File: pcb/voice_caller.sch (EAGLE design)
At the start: 13 parts, among them IC1 MEGA8-AI, IC2 78L12SMD, U1 AT45DB321D-S, X2 RJ45-8L-B

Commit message: Who knows
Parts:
- removed C4: (no value), rcl:C-EUC1206K
- removed IC1: MEGA8-AI, atmel:MEGA8-AI
- removed R3: 220, rcl:R-EU_M1206
- U$1: value MAX4544-EUTSOT23-6 -> NANO-NOISP; device max4544:MAX4544-EUTSOT23-6 -> Arduino-clone:NANO-NOISP
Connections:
- removed net AUDIO: U$1.NO
- removed net MIC_IN: U$1.NC
- removed net MIC_OUT: U$1.COM
- removed net MIC_SWITCH: U$1.IN
- removed net N$2: C4.1, R3.1, U$1.V+
- net +5V: no longer IC1.VCC@1, IC1.VCC@2, R3.2
- net FLASH_CS: no longer IC1.PB2(SS/OC1B)
- net GND: no longer C4.2, IC1.GND, IC1.GND@1, IC1.GND@2, U$1.GND
- net MISO: no longer IC1.PB4(MISO)
- net MOSI: no longer IC1.PB3(MOSI/OC2)
- net SCK: no longer IC1.PB5(SCK)
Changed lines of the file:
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@@
 <?xml version="1.0" encoding="utf-8"?>
 <!DOCTYPE eagle SYSTEM "eagle.dtd">
-<eagle version="7.1.0">
+<eagle version="7.7.0">
 <drawing>
 <settings>
@@
 </classes>
 <parts>
-<part name="IC1" library="atmel" deviceset="MEGA8" device="-AI"/>
 <part name="+8V" library="supply1" deviceset="VCC" device="" value="+8V"/>
 <part name="GND1" library="supply1" deviceset="GND" device=""/>
@@
 <part name="R1" library="rcl" deviceset="R-EU_" device="M1206" value="3k9"/>
 <part name="R2" library="rcl" deviceset="R-EU_" device="M1206" value="2k2"/>
-<part name="U$1" library="max4544" deviceset="MAX4544-EUT" device="SOT23-6"/>
-<part name="R3" library="rcl" deviceset="R-EU_" device="M1206" value="220"/>
-<part name="P+3" library="supply1" deviceset="+5V" device=""/>
-<part name="C4" library="rcl" deviceset="C-EU" device="C1206K"/>
-<part name="GND4" library="supply1" deviceset="GND" device=""/>
-<part name="GND5" library="supply1" deviceset="GND" device=""/>
+<part name="U$1" library="Arduino-clone" deviceset="NANO-NOISP" device=""/>
 </parts>
 <sheets>
@@
 </plain>
 <instances>
-<instance part="IC1" gate="G$1" x="76.2" y="45.72"/>
 <instance part="+8V" gate="VCC" x="25.4" y="99.06"/>
 <instance part="GND1" gate="1" x="25.4" y="81.28"/>
@@
 <instance part="R1" gate="G$1" x="-15.24" y="93.98"/>
 <instance part="R2" gate="G$1" x="-15.24" y="88.9"/>
-<instance part="U$1" gate="G$1" x="15.24" y="137.16"/>
-<instance part="R3" gate="G$1" x="15.24" y="170.18" rot="R90"/>
-<instance part="P+3" gate="1" x="15.24" y="180.34"/>
-<instance part="C4" gate="G$1" x="22.86" y="157.48"/>
-<instance part="GND4" gate="1" x="15.24" y="119.38"/>
-<instance part="GND5" gate="1" x="22.86" y="147.32"/>
+<instance part="U$1" gate="G$1" x="12.7" y="144.78"/>
 </instances>
 <busses>
@@
 <net name="+5V" class="0">
 <segment>
-<pinref part="IC1" gate="G$1" pin="VCC@1"/>
-<wire x1="53.34" y1="35.56" x2="50.8" y2="35.56" width="0.1524" layer="91"/>
-<label x="50.8" y="35.56" size="1.27" layer="95" rot="R180" xref="yes"/>
-</segment>
-<segment>
-<pinref part="IC1" gate="G$1" pin="VCC@2"/>
-<wire x1="53.34" y1="33.02" x2="50.8" y2="33.02" width="0.1524" layer="91"/>
-<label x="50.8" y="33.02" size="1.27" layer="95" rot="R180" xref="yes"/>
-</segment>
-<segment>
 <pinref part="P+2" gate="1" pin="+5V"/>
 <pinref part="C2" gate="G$1" pin="1"/>
@@
 <wire x1="48.26" y1="96.52" x2="48.26" y2="93.98" width="0.1524" layer="91"/>
 </segment>
-<segment>
-<pinref part="R3" gate="G$1" pin="2"/>
-<wire x1="15.24" y1="175.26" x2="15.24" y2="177.8" width="0.1524" layer="91"/>
-<pinref part="P+3" gate="1" pin="+5V"/>
-</segment>
 </net>
 <net name="GND" class="0">
-<segment>
-<pinref part="IC1" gate="G$1" pin="GND@1"/>
-<wire x1="53.34" y1="40.64" x2="50.8" y2="40.64" width="0.1524" layer="91"/>
-<label x="50.8" y="40.64" size="1.27" layer="95" rot="R180" xref="yes"/>
-</segment>
-<segment>
-<pinref part="IC1" gate="G$1" pin="GND@2"/>
-<wire x1="53.34" y1="38.1" x2="50.8" y2="38.1" width="0.1524" layer="91"/>
-<label x="50.8" y="38.1" size="1.27" layer="95" rot="R180" xref="yes"/>
-</segment>
 <segment>
 <pinref part="GND1" gate="1" pin="GND"/>
@@
 </segment>
 <segment>
-<pinref part="IC1" gate="G$1" pin="GND"/>
-<wire x1="53.34" y1="66.04" x2="50.8" y2="66.04" width="0.1524" layer="91"/>
-<label x="50.8" y="66.04" size="1.27" layer="95" rot="R180" xref="yes"/>
-</segment>
-<segment>
 <pinref part="U1" gate="G$1" pin="GND"/>
 <wire x1="172.72" y1="63.5" x2="175.26" y2="63.5" width="0.1524" layer="91"/>
@@
 <label x="-25.4" y="48.26" size="1.016" layer="95" xref="yes"/>
 </segment>
-<segment>
-<pinref part="U$1" gate="G$1" pin="GND"/>
-<wire x1="15.24" y1="124.46" x2="15.24" y2="121.92" width="0.1524" layer="91"/>
-<pinref part="GND4" gate="1" pin="GND"/>
-</segment>
-<segment>
-<pinref part="GND5" gate="1" pin="GND"/>
-<pinref part="C4" gate="G$1" pin="2"/>
-<wire x1="22.86" y1="149.86" x2="22.86" y2="152.4" width="0.1524" layer="91"/>
-</segment>
 </net>
 <net name="VCC" class="0">
@@
 <net name="MOSI" class="0">
 <segment>
-<pinref part="IC1" gate="G$1" pin="PB3(MOSI/OC2)"/>
 <wire x1="101.6" y1="17.78" x2="104.14" y2="17.78" width="0.1524" layer="91"/>
 <label x="104.14" y="17.78" size="1.016" layer="95" xref="yes"/>
@@
 <net name="MISO" class="0">
 <segment>
-<pinref part="IC1" gate="G$1" pin="PB4(MISO)"/>
 <wire x1="101.6" y1="15.24" x2="104.14" y2="15.24" width="0.1524" layer="91"/>
 <label x="104.14" y="15.24" size="1.016" layer="95" xref="yes"/>
@@
 <net name="SCK" class="0">
 <segment>
-<pinref part="IC1" gate="G$1" pin="PB5(SCK)"/>
 <wire x1="101.6" y1="12.7" x2="104.14" y2="12.7" width="0.1524" layer="91"/>
 <label x="104.14" y="12.7" size="1.016" layer="95" xref="yes"/>
@@
 </segment>
 <segment>
-<pinref part="IC1" gate="G$1" pin="PB2(SS/OC1B)"/>
 <wire x1="101.6" y1="20.32" x2="104.14" y2="20.32" width="0.1524" layer="91"/>
 <label x="104.14" y="20.32" size="1.016" layer="95" xref="yes"/>
@@
 </segment>
 </net>
-<net name="N$2" class="0">
-<segment>
-<pinref part="U$1" gate="G$1" pin="V+"/>
-<wire x1="15.24" y1="149.86" x2="15.24" y2="162.56" width="0.1524" layer="91"/>
-<pinref part="R3" gate="G$1" pin="1"/>
-<pinref part="C4" gate="G$1" pin="1"/>
-<wire x1="15.24" y1="162.56" x2="15.24" y2="165.1" width="0.1524" layer="91"/>
-<wire x1="22.86" y1="160.02" x2="22.86" y2="162.56" width="0.1524" layer="91"/>
-<wire x1="22.86" y1="162.56" x2="15.24" y2="162.56" width="0.1524" layer="91"/>
-<junction x="15.24" y="162.56"/>
-</segment>
-</net>
-<net name="MIC_OUT" class="0">
-<segment>
-<pinref part="U$1" gate="G$1" pin="COM"/>
-<wire x1="35.56" y1="142.24" x2="38.1" y2="142.24" width="0.1524" layer="91"/>
-<label x="38.1" y="142.24" size="1.016" layer="95" xref="yes"/>
-</segment>
-</net>
-<net name="MIC_SWITCH" class="0">
-<segment>
-<pinref part="U$1" gate="G$1" pin="IN"/>
-<wire x1="35.56" y1="134.62" x2="38.1" y2="134.62" width="0.1524" layer="91"/>
-<label x="38.1" y="134.62" size="1.016" layer="95" xref="yes"/>
-</segment>
-</net>
-<net name="AUDIO" class="0">
-<segment>
-<pinref part="U$1" gate="G$1" pin="NO"/>
-<wire x1="-5.08" y1="134.62" x2="-7.62" y2="134.62" width="0.1524" layer="91"/>
-<label x="-7.62" y="134.62" size="1.016" layer="95" rot="R180" xref="yes"/>
-</segment>
-</net>
-<net name="MIC_IN" class="0">
-<segment>
-<pinref part="U$1" gate="G$1" pin="NC"/>
-<wire x1="-5.08" y1="142.24" x2="-7.62" y2="142.24" width="0.1524" layer="91"/>
-<label x="-7.62" y="142.24" size="1.016" layer="95" rot="R180" xref="yes"/>
-</segment>
-</net>

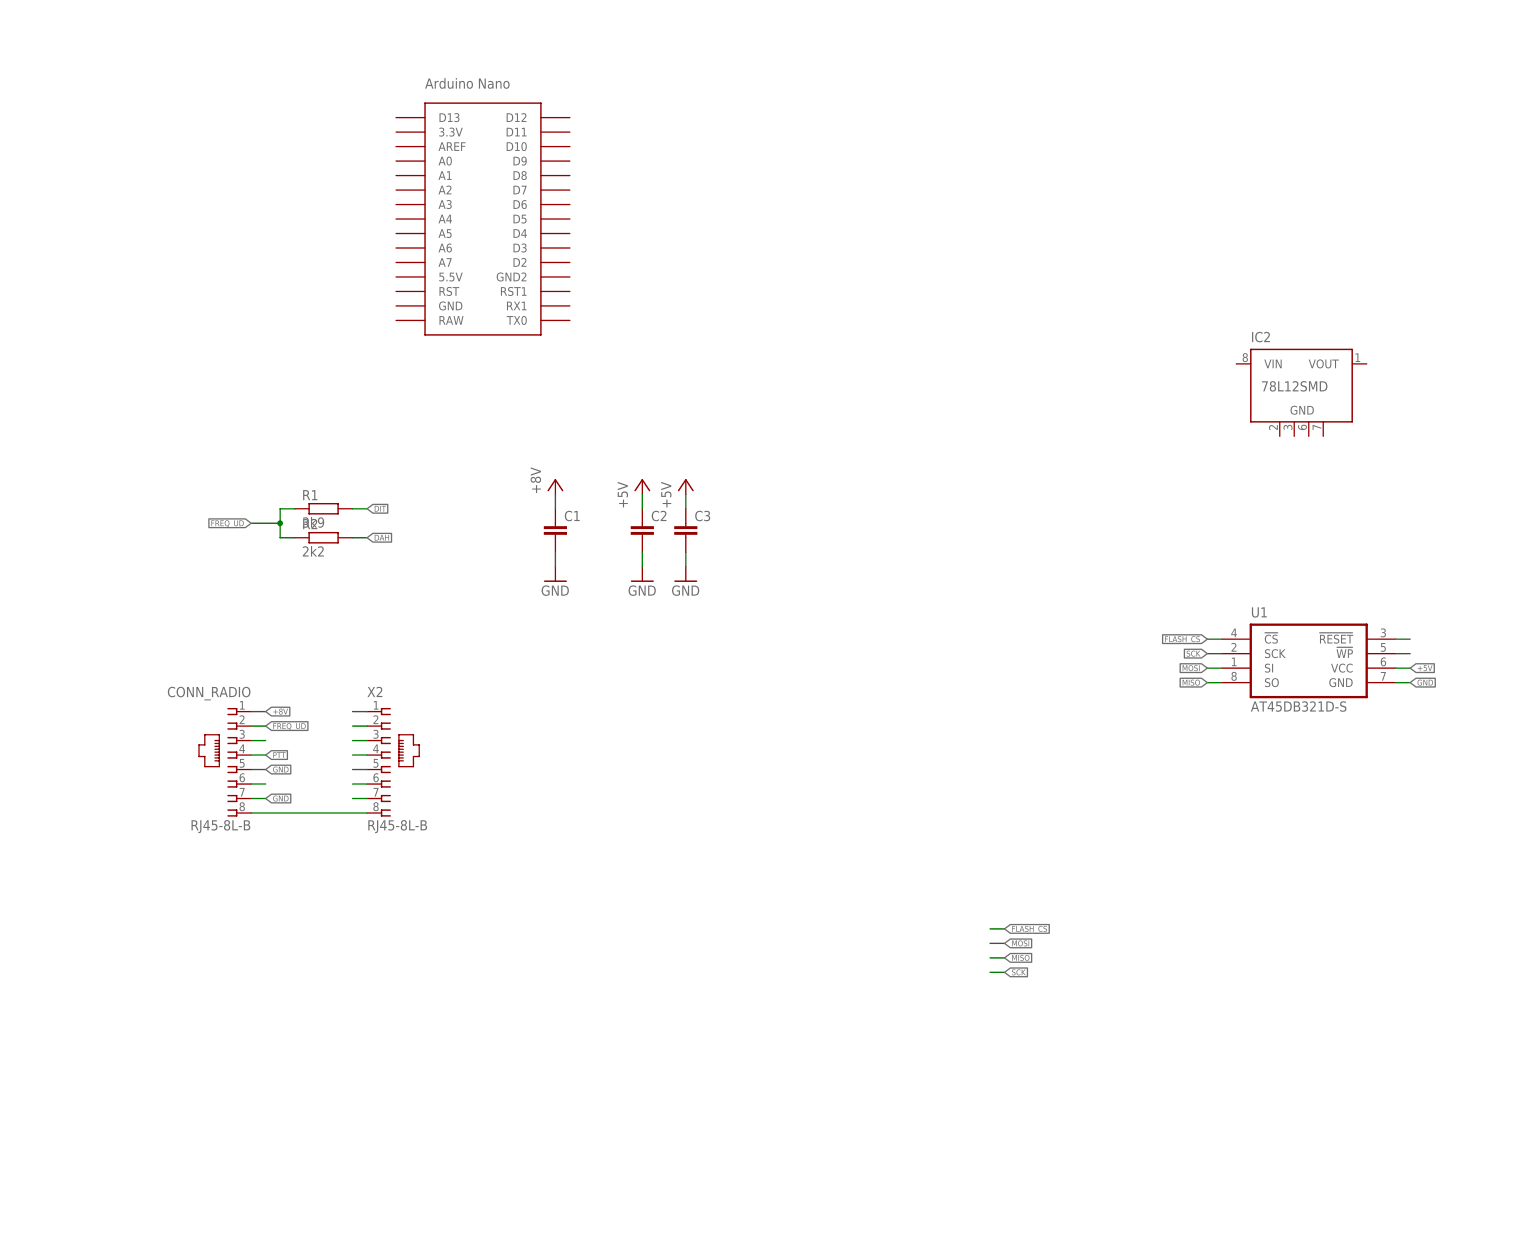
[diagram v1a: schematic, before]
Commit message: Nano changed to pro micro
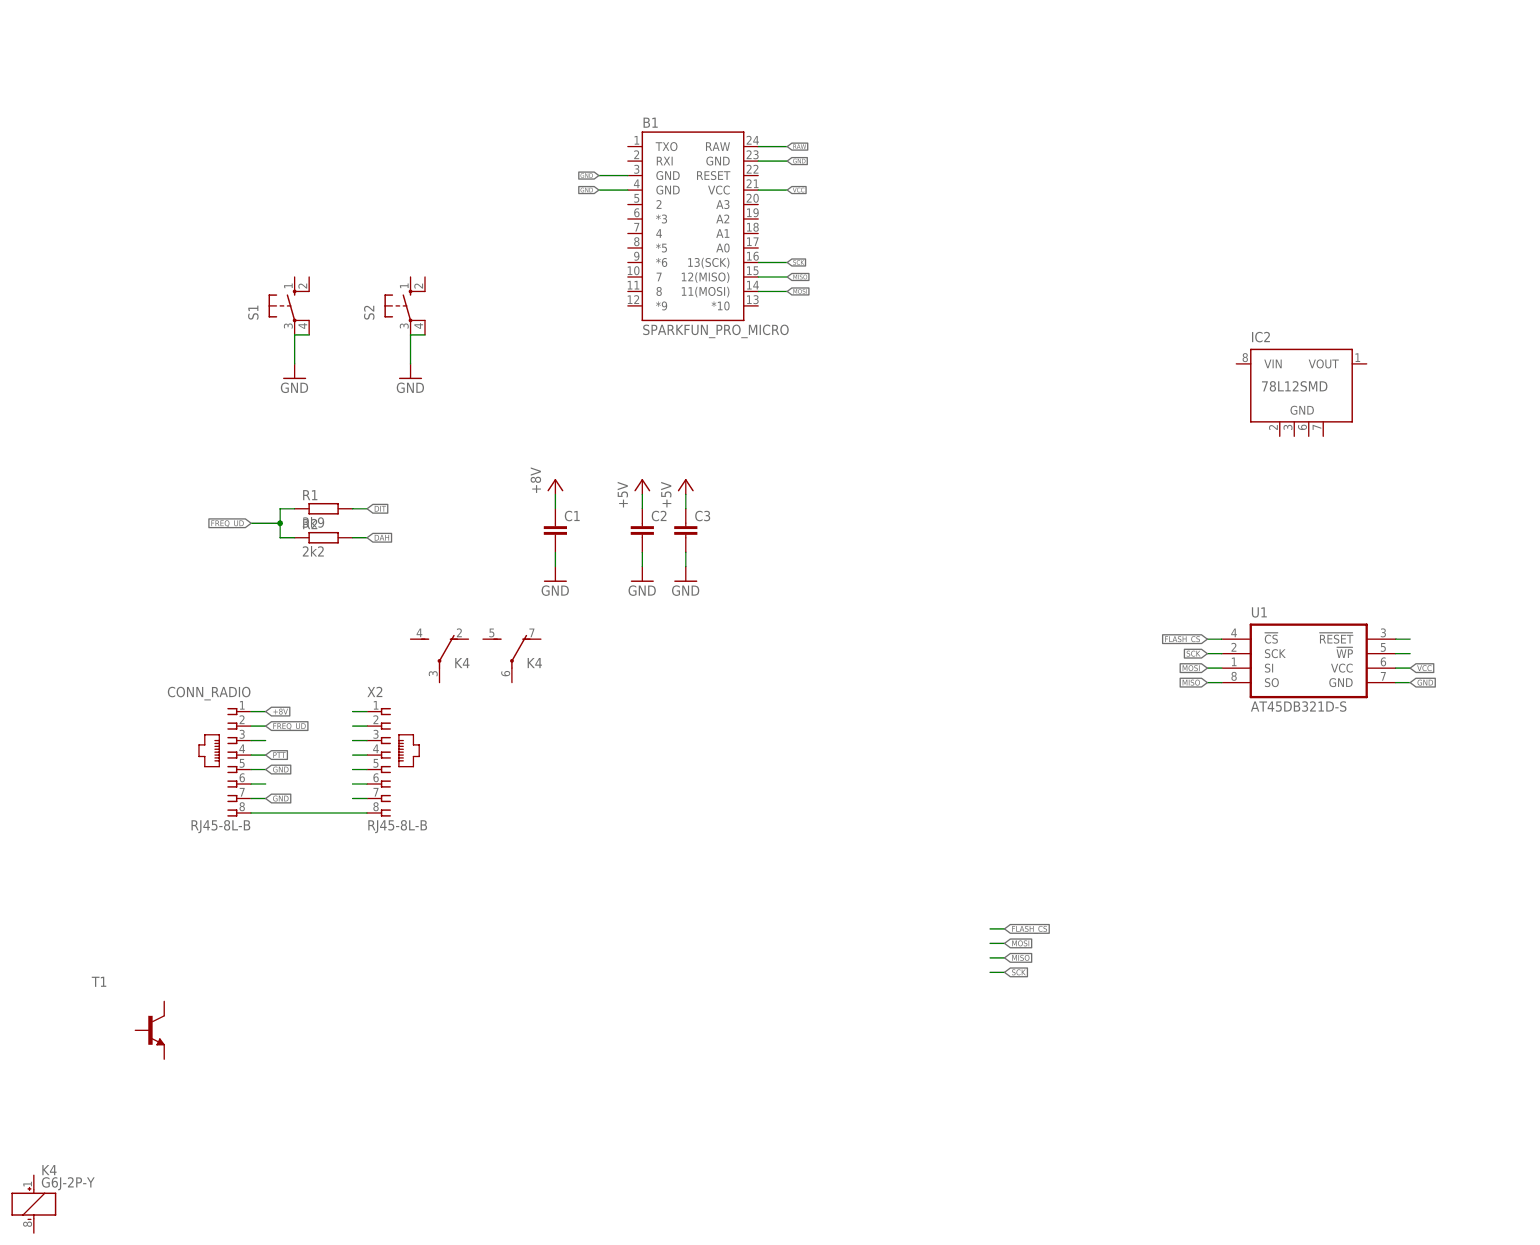
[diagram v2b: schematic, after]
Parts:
- removed U$1: NANO-NOISP, Arduino-clone:NANO-NOISP
- added B1: SPARKFUN_PRO_MICRO, SparkFun-Boards:SPARKFUN_PRO_MICRO
- added K4: G6J-2P-Y, relay:G6J-2P-Y
- added S1, S2: (no value), switch-omron:10-XX
- added T1: (no value), transistor:MMBT3904LT1-NPN-SOT23-BEC
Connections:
- new net RAW: B1.RAW
- net +5V: no longer U1.VCC
- net GND: now also B1.GND, B1.GND@1, B1.GND@2, S1.P, S1.P1, S2.P, S2.P1
- net MISO: now also B1.12(MISO)
- net MOSI: now also B1.11(MOSI)
- net SCK: now also B1.13(SCK)
- net VCC: now also B1.VCC, U1.VCC

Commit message: RJ-45 connected
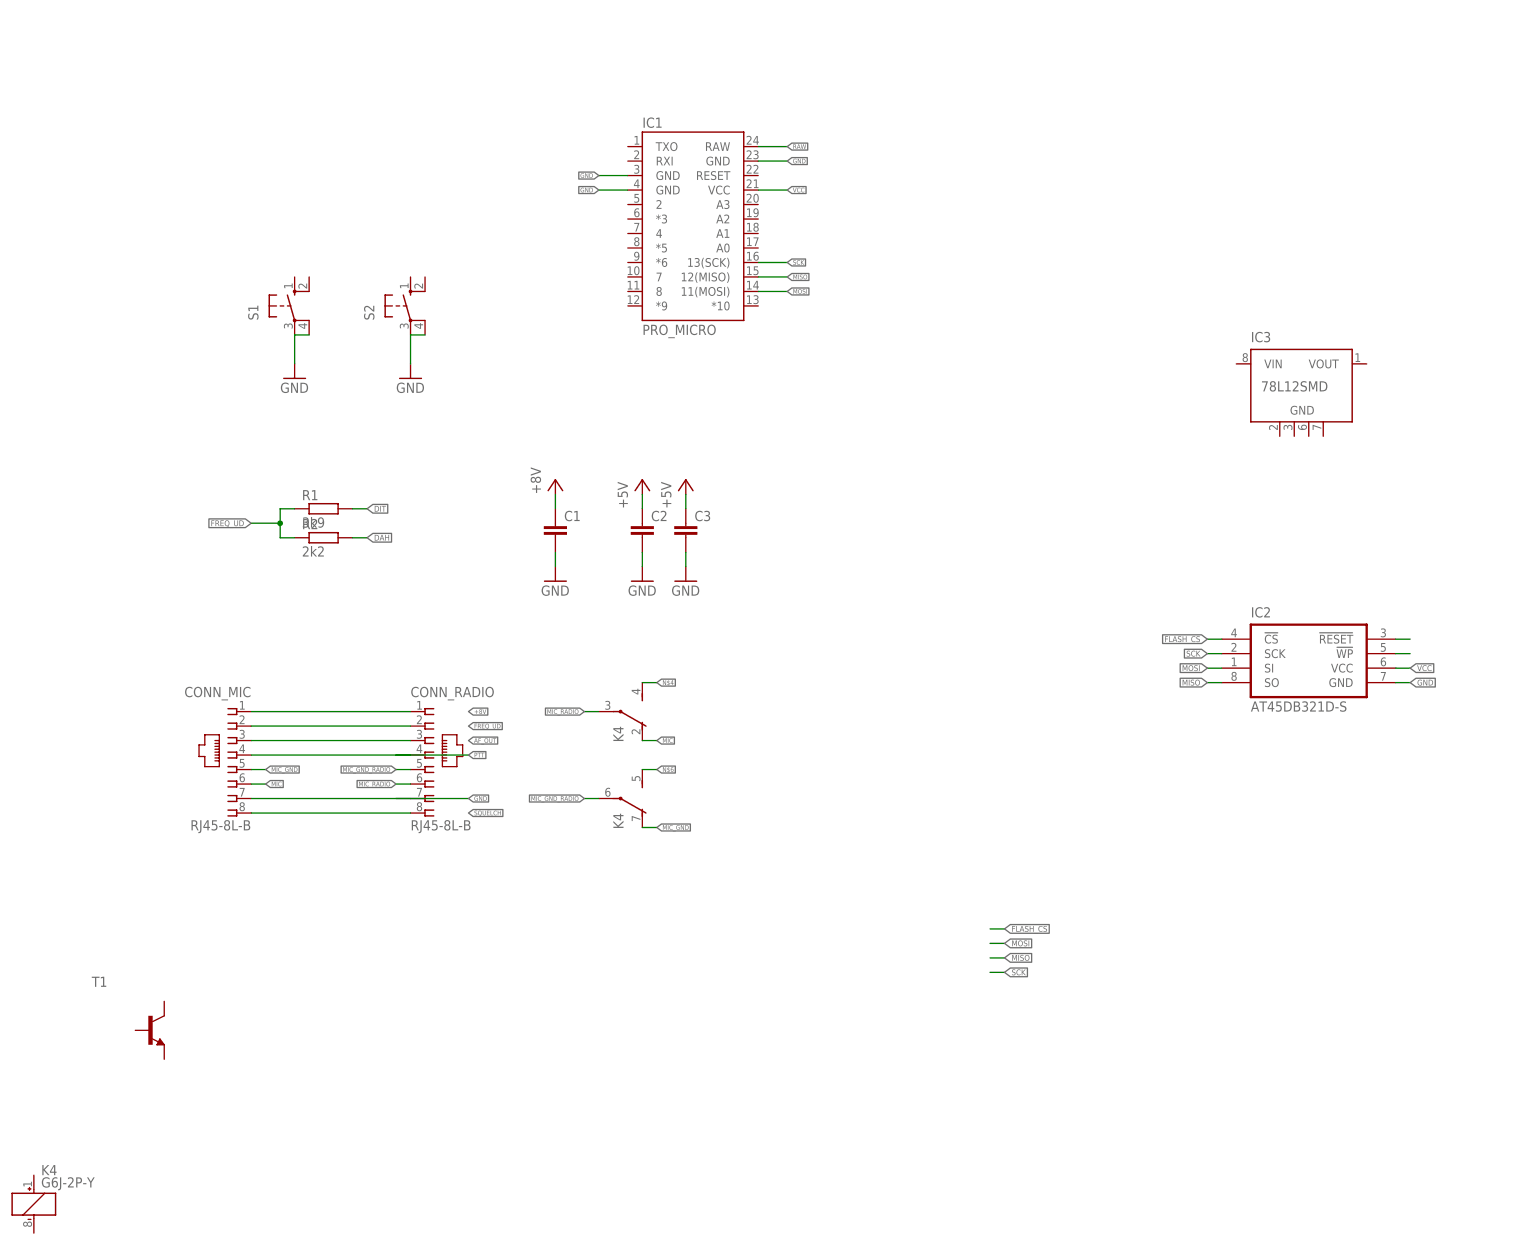
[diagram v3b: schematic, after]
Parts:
- removed U1: AT45DB321D-S, memory-atmel:AT45DB321D-S
- removed X2: RJ45-8L-B, con-tycoelectronics:RJ45-8L-B
- added CONN_MIC: RJ45-8L-B, con-tycoelectronics:RJ45-8L-B
- added IC3: 78L12SMD, linear:78L12SMD
- IC1: value SPARKFUN_PRO_MICRO -> PRO_MICRO
- IC2: value 78L12SMD -> AT45DB321D-S; device linear:78L12SMD -> memory-atmel:AT45DB321D-S
- renumbered B1 to IC1
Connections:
- removed net N$1: CONN_RADIO.8, X2.8
- removed net N$10: CONN_RADIO.3
- removed net N$11: X2.3
- removed net N$12: CONN_RADIO.6
- removed net N$13: X2.6
- removed net N$9: X2.1
- new net AF_OUT: CONN_MIC.3, CONN_RADIO.3
- new net MIC: CONN_MIC.6, K42.O
- new net MIC_GND: CONN_MIC.5, K43.O
- new net MIC_GND_RADIO: CONN_RADIO.5, K43.P
- new net MIC_RADIO: CONN_RADIO.6, K42.P
- new net SQUELCH: CONN_MIC.8, CONN_RADIO.8
- net +8V: now also CONN_MIC.1
- net FLASH_CS: now also IC2.!CS!; no longer U1.!CS!
- net FREQ_UD: now also CONN_MIC.2
- net GND: now also CONN_MIC.7, IC2.GND; no longer CONN_RADIO.5, CONN_RADIO.7, U1.GND
- net MISO: now also IC2.SO; no longer U1.SO
- net MOSI: now also IC2.SI; no longer U1.SI
- net N$3: now also CONN_RADIO.7; no longer X2.7
- net N$4: now also K42.S; no longer X2.5
- net N$5: now also CONN_RADIO.4; no longer X2.4
- net N$6: now also K43.S; no longer X2.2
- net N$7: now also IC2.!WP!; no longer U1.!WP!
- net N$8: now also IC2.!RESET!; no longer U1.!RESET!
- net PTT: now also CONN_MIC.4; no longer CONN_RADIO.4
- net SCK: now also IC2.SCK; no longer U1.SCK
- net VCC: now also IC2.VCC; no longer U1.VCC
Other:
- moved on the sheet: CONN_RADIO, K4

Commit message: Some progress with the PCB
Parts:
- added C4, C5, C6: (no value), rcl:C-EUC1206K
- added R3, R5, R6: (no value), rcl:R-EU_M1206
- added R4: (no value), rcl:R-TRIMMT93XB
- added R7: 1k, rcl:R-EU_M1206
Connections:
- removed net RAW: IC1.RAW
- removed net VCC: C1.1, IC1.VCC, IC2.VCC
- new net +3V3: IC1.VCC, IC2.VCC
- new net MIC_PWM: K42.S, R5.2, R6.2
- new net N$1: C4.2, R3.1
- new net N$2: C5.2, R3.2, R4.E
- new net N$9: R7.2, T1.B
- new net PWM: C4.1, IC1.*10
- net +5V: now also IC1.RAW, IC3G$1.VOUT, K41.+
- net +8V: now also C1.1, IC3G$1.VIN
- net GND: now also C5.1, CONN_RADIO.7, IC3G$1.GND@1, IC3G$1.GND@2, IC3G$1.GND@3, IC3G$1.GND@4, K43.S, R4.A, R6.1, T1.E
- net N$3: now also C6.2, R5.1; no longer CONN_RADIO.7
- net N$4: now also K41.-, T1.C; no longer K42.S
- net N$6: now also C6.1, R4.S; no longer K43.S
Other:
- moved on the sheet: K4, R1, T1
